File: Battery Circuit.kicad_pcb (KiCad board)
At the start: 2 copper layers, 36.4 x 39.7 mm, 43 parts, among them J1 1827685-4, J2 Programming Header (SWD), Q1 Si2309DS, Q2 BC847, SW1 SW_Push, U1 TPS54202DDC, U2 STM32G071KBUxN

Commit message: Fixed the warning
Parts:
- R12: value 22.1kΩ -> 32.4kΩ
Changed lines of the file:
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@@
 			)
 		)
-		(property "Value" "22.1kΩ"
+		(property "Value" "32.4kΩ"
 			(at 0 1.17 0)
 			(layer "F.Fab")

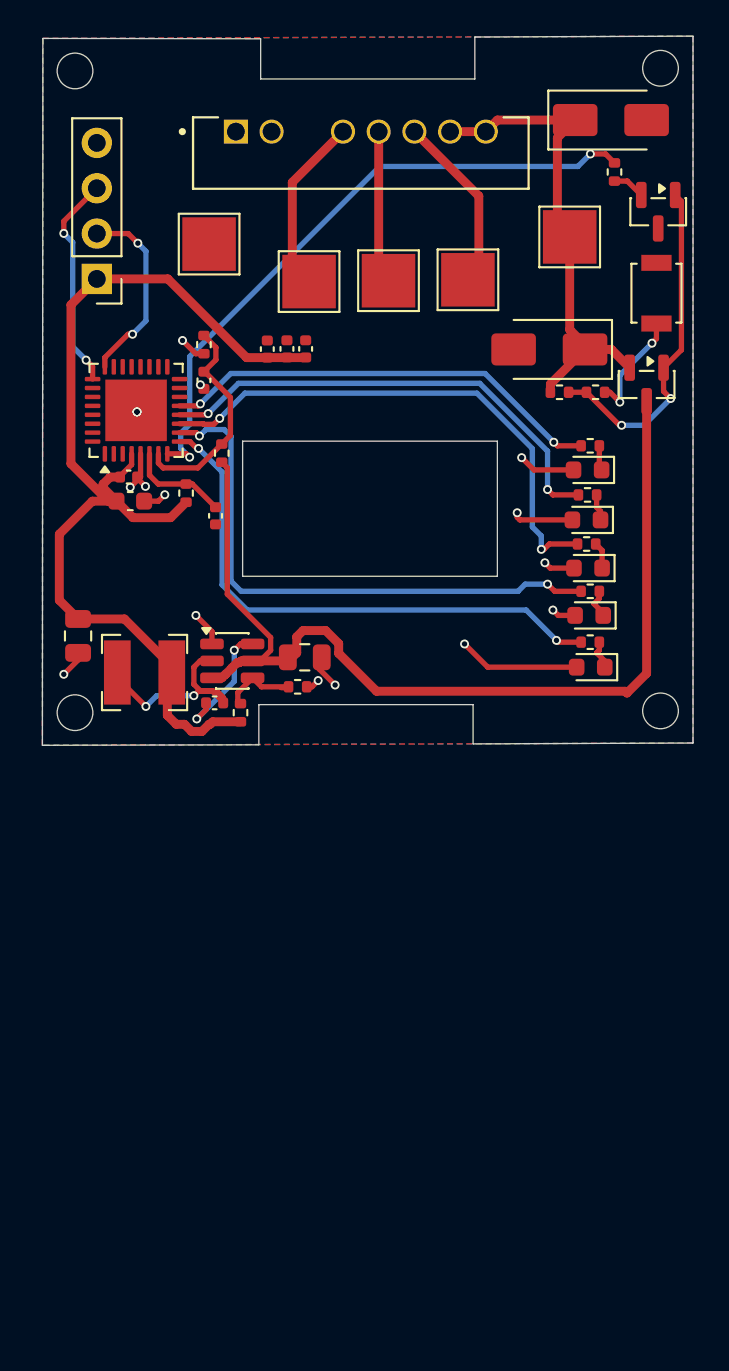
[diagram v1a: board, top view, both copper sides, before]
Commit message: Finalize 4-layer PCB layout: implement 20A top/bottom copper pours, add via stitching, addition of thermistor and clear all DRC violations.
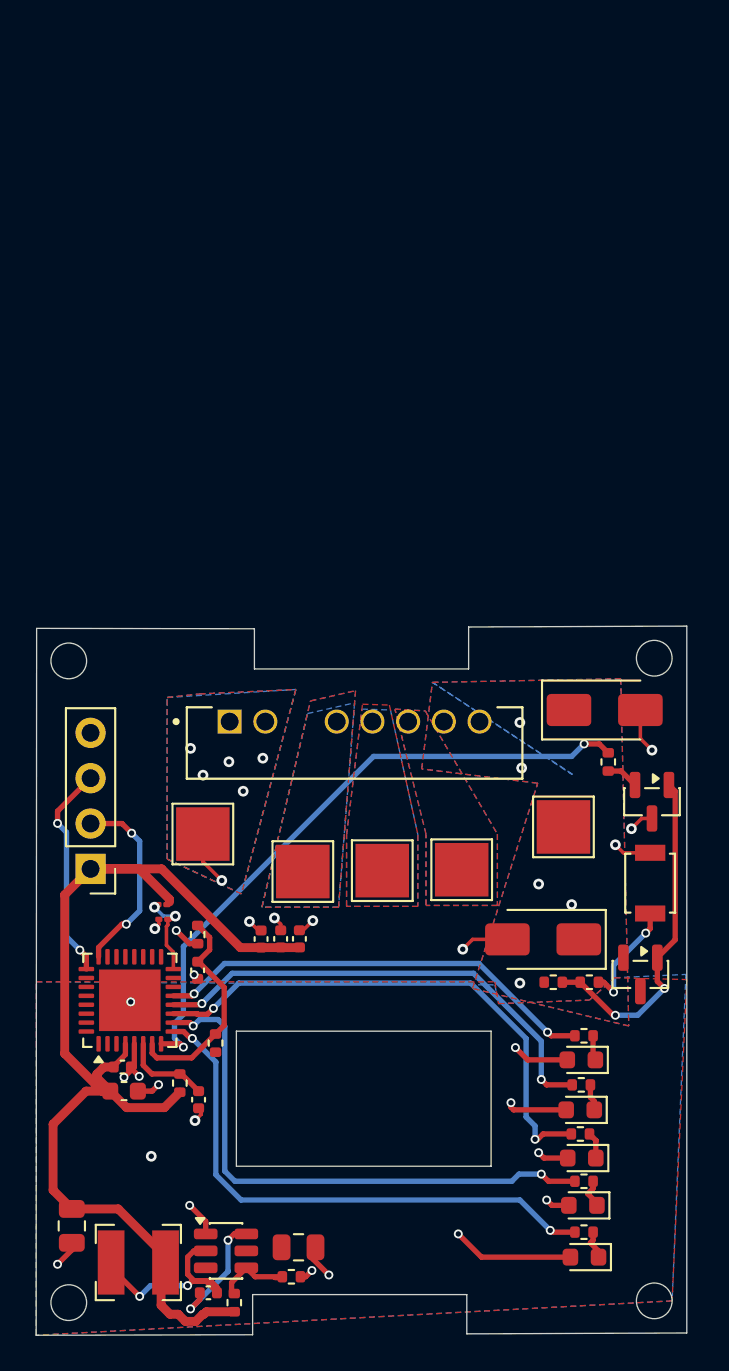
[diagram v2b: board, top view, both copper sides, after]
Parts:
- added R14: 10k, Resistor_SMD:R_01005_0402Metric, F.Cu at (134.5, 104.3)
- added TH1: Thermistor_NTC_10k, Resistor_SMD:R_01005_0402Metric, F.Cu at (134.6, 105.2)
- moved L1 33.1 mm to (133.2, 124.4)
- moved Q2 33.1 mm to (161.9, 98.6)
- moved R11 33.1 mm to (138.6, 126.7)
- moved SW1 33.1 mm to (161.8, 103.2)
- moved U2 33.1 mm to (132.7, 109.7)
- moved D2 33.1 mm to (159.3, 93.5)
- moved J1 33.1 mm to (138.3, 94.1)
- moved C1 33.1 mm to (137.1, 126.1)
- moved C10 33.1 mm to (129.4, 122.3)
- moved C2 33.1 mm to (132.3, 113.5)
- moved C3 33.1 mm to (141.2, 106.3)
- moved C4 33.1 mm to (142.2, 106.3)
- moved C5 33.1 mm to (140.1, 106.3)
- moved C6 33.1 mm to (136.5, 108.0)
- moved C8 33.1 mm to (132.4, 114.8)
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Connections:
- U2 pad 16: unconnected-(U2-PB1-Pad16) -> /TEMP_SENSE
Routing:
- net /+4S_SW: track 56.6 -> 0.22 mm, vias 0 -> 1
- net /+4S_PROT: track 27.3 -> 0.17 mm, vias 0 -> 5
- net GND: track 28.4 -> 45.1 mm, vias 16 -> 30
- net Net-(J1-Pad5): track 10.0 -> 0.00 mm
- net Net-(J1-Pad3): track 9.97 -> 0.00 mm
- net Net-(J1-Pad4): track 8.58 -> 0.00 mm
- net /+3V3: track 60.6 -> 65.9 mm
- net /TEMP_SENSE: track 0.00 -> 5.11 mm, vias 0 -> 2
- net Net-(U2-PF2): track 5.64 -> 4.90 mm
- added copper zone on B.Cu, net /+4S_PROT
- added copper zone on F.Cu, net /+4S_PROT
- added copper zone on B.Cu, net /+4S_SW
- added copper zone on F.Cu, net /+4S_SW
- added copper zone on In1.Cu, net GND
- added copper zone on In2.Cu, net GND
- added copper zone on B.Cu, net Net-(J1-Pad3)
- added copper zone on F.Cu, net Net-(J1-Pad3)
- added copper zone on B.Cu, net Net-(J1-Pad4)
- added copper zone on F.Cu, net Net-(J1-Pad4)
- added copper zone on B.Cu, net Net-(J1-Pad5)
- added copper zone on F.Cu, net Net-(J1-Pad5)
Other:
- copper layers 2 -> 4

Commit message: feat(system): implement BMS firmware
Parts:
- D5, D6: value Blue -> Green
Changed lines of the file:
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@@
 			)
 		)
-		(property "Value" "Blue"
+		(property "Value" "Green"
 			(at 0 1.43 0)
 			(layer "F.Fab")
@@
 			)
 		)
-		(property "Value" "Blue"
+		(property "Value" "Green"
 			(at 0 1.43 0)
 			(layer "F.Fab")
@@
 		)
 	)
-	(group ""
-		(members "0a004f0c-470b-4d08-906b-5c359fbb434e" "6f456ec9-d39b-4d39-af0d-d1c9770db869"
-			"903ecc9e-f5b2-494d-ac4c-62453744a50d" "a3816e48-3ce3-4a7b-b6f8-05a8cdf704b8"
-			"d12ee226-368a-4dee-bd1c-65814e7010f1" "d44153d5-9140-40ca-be6c-89fa441412da"
-			"e38b0a4b-40db-4308-99b4-2d334da7dc17" "e5b5006f-bbca-4032-a89b-64f35cc98941"
-			"fe8c93e3-1548-4acd-a021-e908c11a5ef3" "ff5a212c-d25b-4c00-ae8b-297f4813fe8f"
-		)
-	)

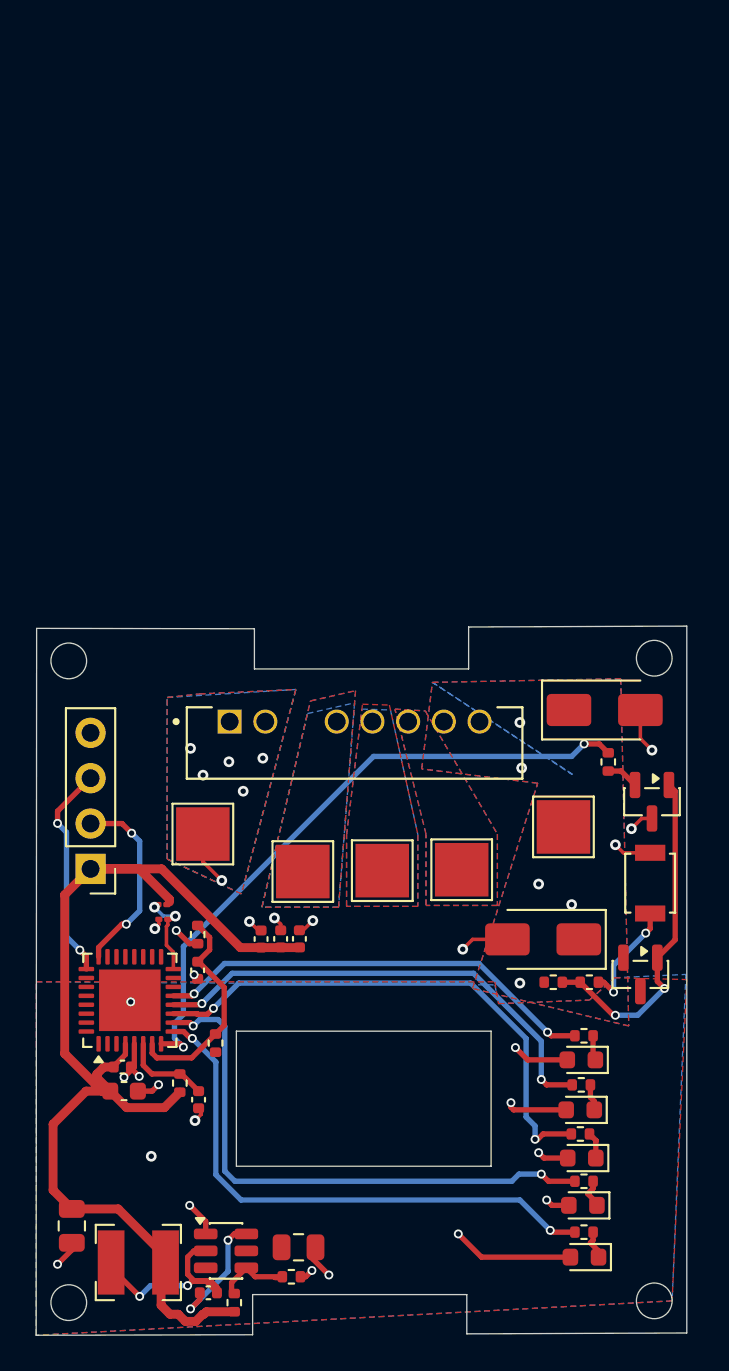
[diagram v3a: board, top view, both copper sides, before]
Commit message: feat(system): GERBER File & BOM with STM32G071GBU6N MCU
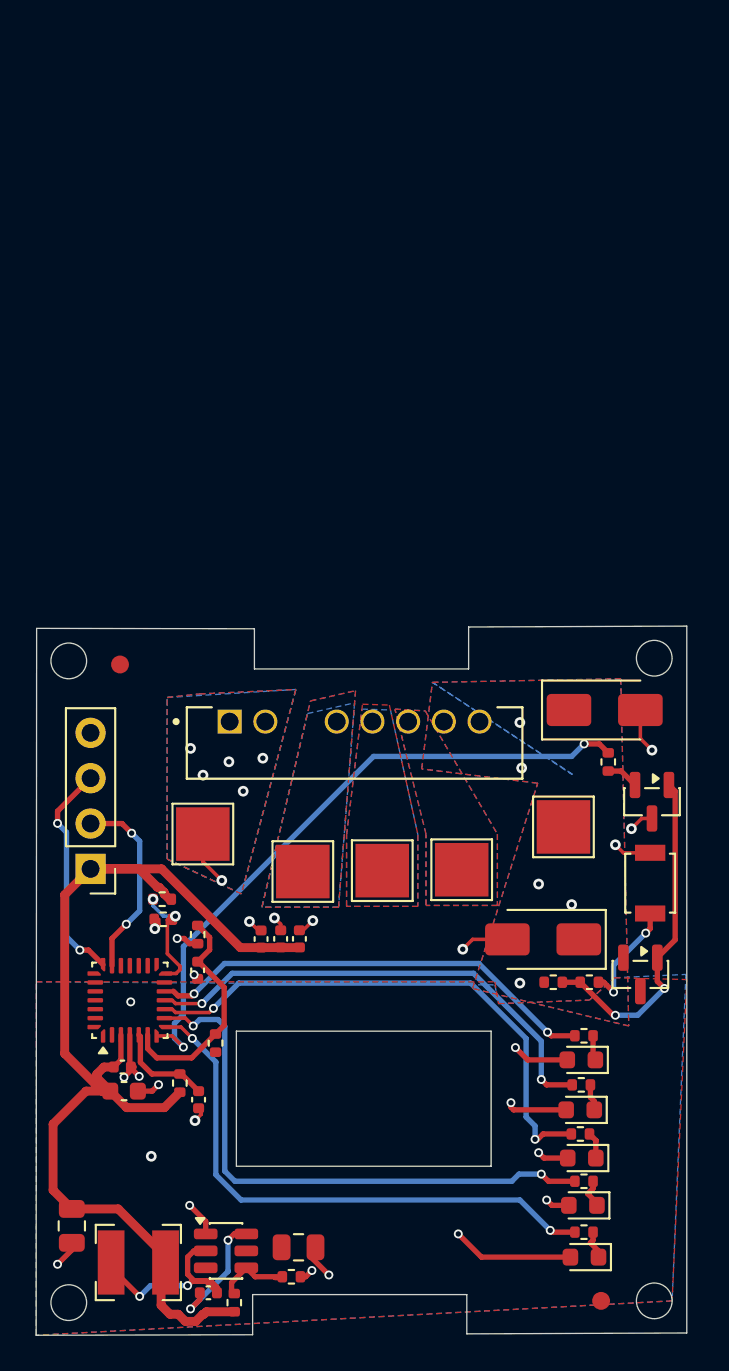
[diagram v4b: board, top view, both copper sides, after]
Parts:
- added FID1: Fiducial, Fiducial:Fiducial_1mm_Mask2mm, F.Cu at (132.2, 90.9)
- added FID2: Fiducial, Fiducial:Fiducial_1mm_Mask2mm, F.Cu at (159.1, 126.5)
- R1, R2, R3, R4, R5: value 270Ω -> 120Ω
- R14, TH1: footprint Resistor_SMD:R_01005_0402Metric -> Resistor_SMD:R_0402_1005Metric
- U2: value STM32G071KBUxN -> STM32G071GBUxN; footprint Package_DFN_QFN:QFN-32-1EP_5x5mm_P0.5mm_EP3.45x3.45mm -> Package_DFN_QFN:QFN-28_4x4mm_P0.5mm
- moved R14 0.30 mm to (134.5, 104.0)
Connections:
- U2 pad 10: Net-(U2-PA3) -> Net-(U2-PA4)
- U2 pad 11: Net-(U2-PA4) -> Net-(U2-PA5)
- U2 pad 12: Net-(U2-PA5) -> Net-(U2-PA6)
- U2 pad 13: Net-(U2-PA6) -> unconnected-(U2-PA7-Pad13)
- U2 pad 14: unconnected-(U2-PA7-Pad14) -> /TEMP_SENSE
- U2 pad 16: /TEMP_SENSE -> unconnected-(U2-PA8-Pad16)
- U2 pad 20: unconnected-(U2-PC6-Pad20) -> /SWDIO
- U2 pad 21: unconnected-(U2-PA10/UCPD1_DBCC2-Pad21) -> /SWCLK
- U2 pad 24: /SWDIO -> unconnected-(U2-PD2-Pad24)
- U2 pad 25: /SWCLK -> unconnected-(U2-PD3-Pad25)
- U2 pad 3: unconnected-(U2-PC15-Pad3) -> /+3V3
- U2 pad 4: /+3V3 -> GND
- U2 pad 5: GND -> Net-(U2-PF2)
- U2 pad 6: Net-(U2-PF2) -> /BATT_SENSE
- U2 pad 7: /BATT_SENSE -> /LATCH_HOLD
- U2 pad 8: /LATCH_HOLD -> Net-(U2-PA2)
- U2 pad 9: Net-(U2-PA2) -> Net-(U2-PA3)
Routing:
- net /TEMP_SENSE: track 5.11 -> 6.45 mm
- net Net-(U2-PA2): track 30.8 -> 31.5 mm
- net Net-(U2-PA5): track 26.9 -> 27.6 mm
- net Net-(U2-PF2): track 4.90 -> 5.50 mm
- net /BATT_SENSE: track 12.2 -> 12.8 mm
- net Net-(U2-PA3): track 31.6 -> 32.2 mm
- net Net-(U2-PA4): track 29.8 -> 30.3 mm

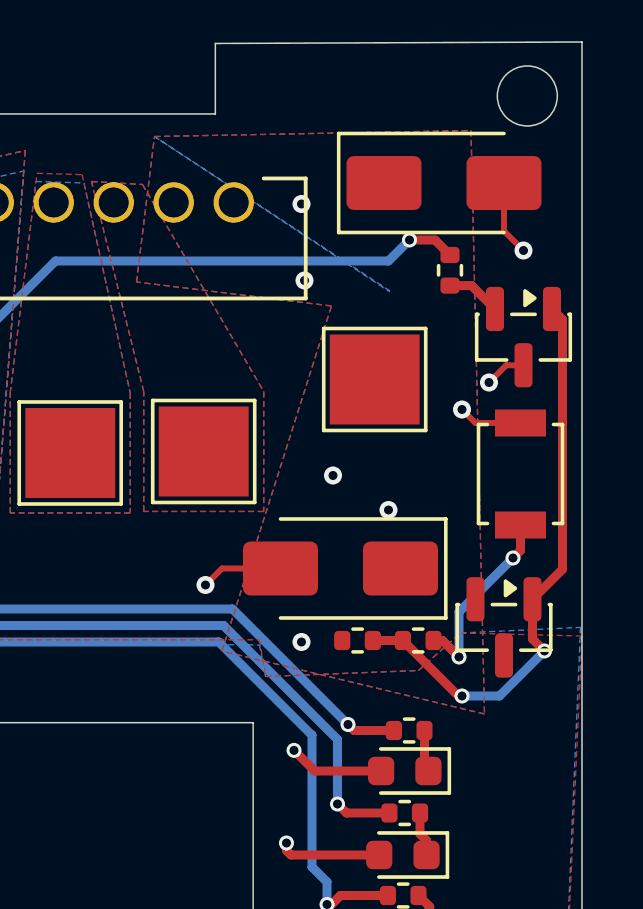
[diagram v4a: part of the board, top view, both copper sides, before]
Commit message: Update hardware schematic to Rev 1.1 (fixed MOSFET/drain)
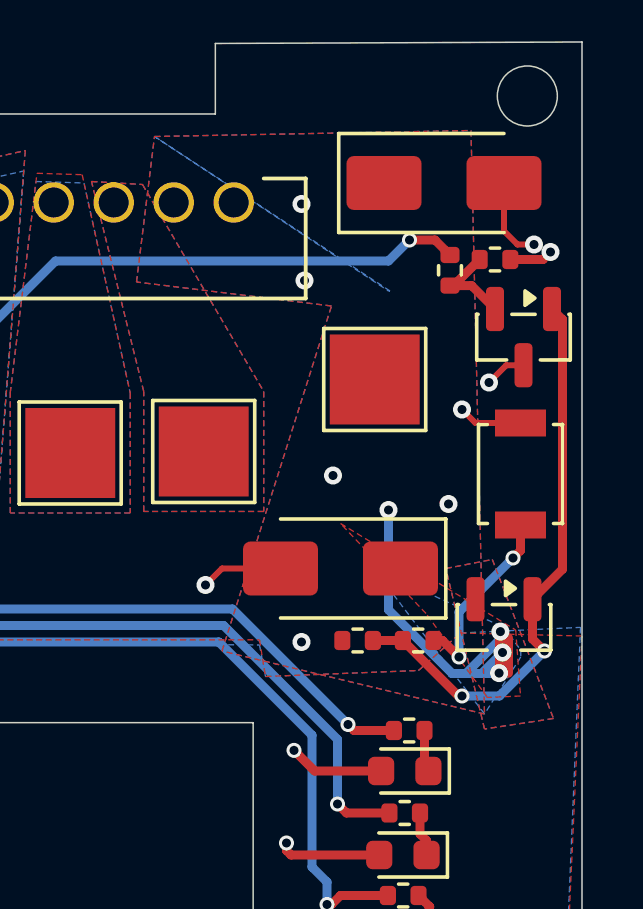
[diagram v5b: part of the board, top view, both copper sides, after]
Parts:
- added R15: 10k, Resistor_SMD:R_0402_1005Metric, F.Cu at (161.0, 96.0)
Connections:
- Q1 pad 2: /+4S_PROT -> /+4S_SW
- Q1 pad 3: /+4S_SW -> /+4S_PROT
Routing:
- net /+4S_PROT: track 0.17 -> 13.5 mm, vias 5 -> 9
- net GND: track 45.4 -> 47.1 mm, vias 30 -> 31
- net Net-(Q2-B): track 1.82 -> 3.17 mm
